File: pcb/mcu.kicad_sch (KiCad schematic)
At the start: 20 parts, among them U3 IC_MCU_STM32F100C4T6B_48LQFP, X1 XTAL_8M_20PPM_18pF_ECS-80-18-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, X2 XTAL_32K768_10PPM_7pF_ECS-.32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

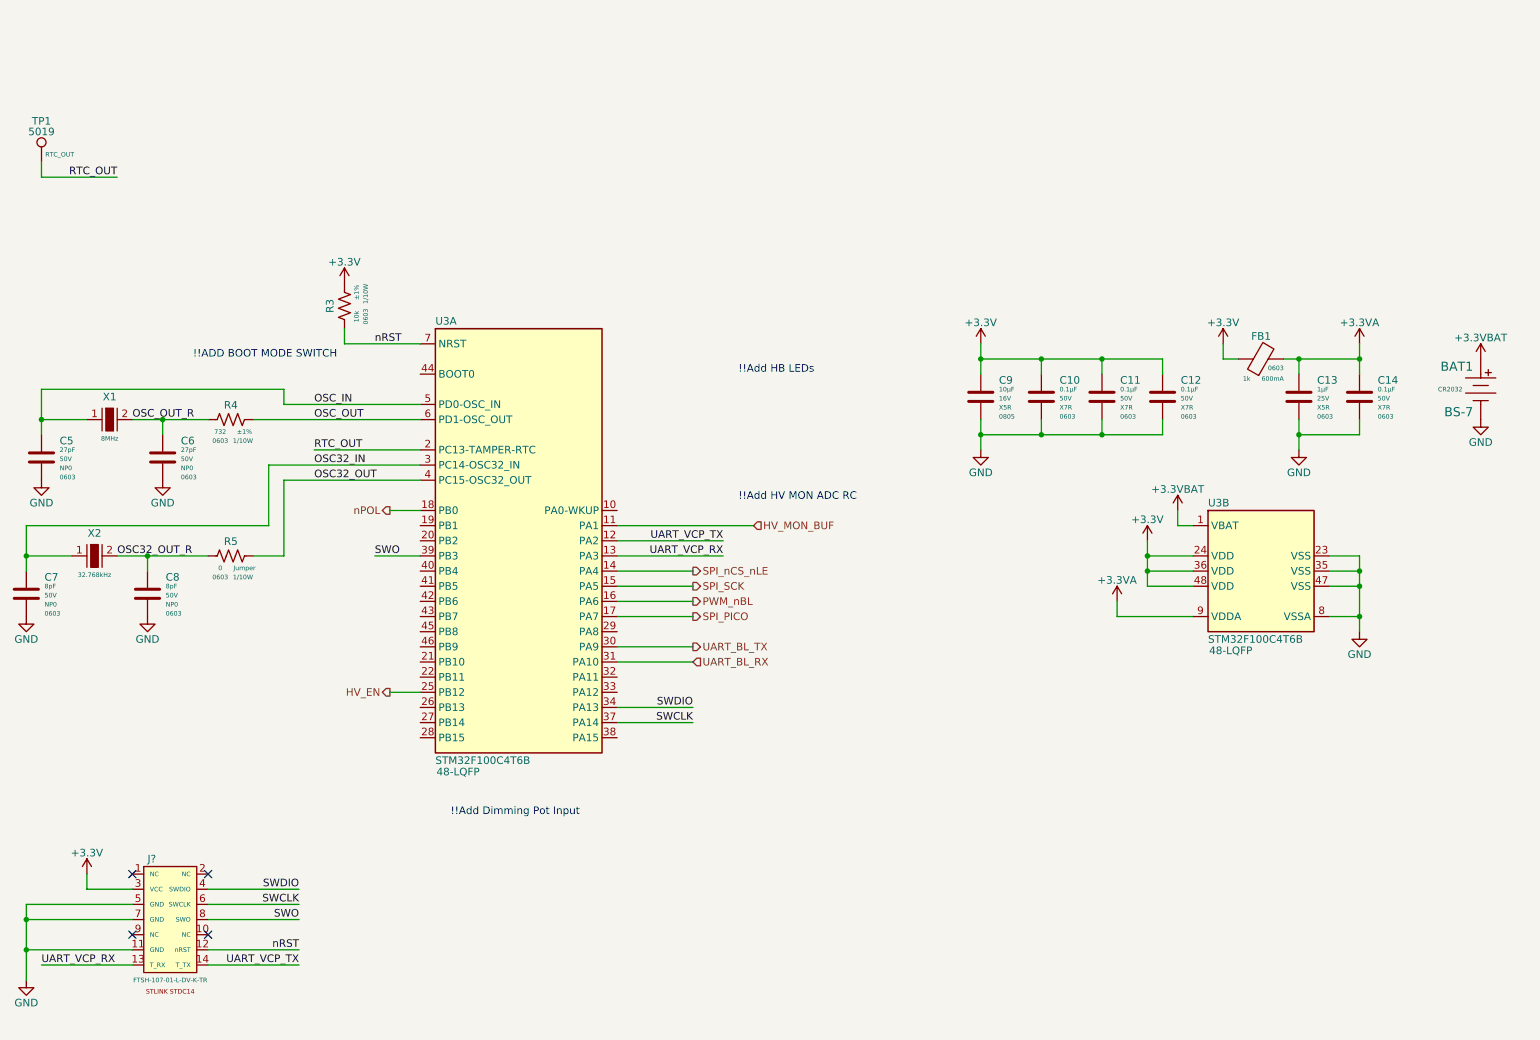
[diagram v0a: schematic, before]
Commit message: Added Boot mode selection
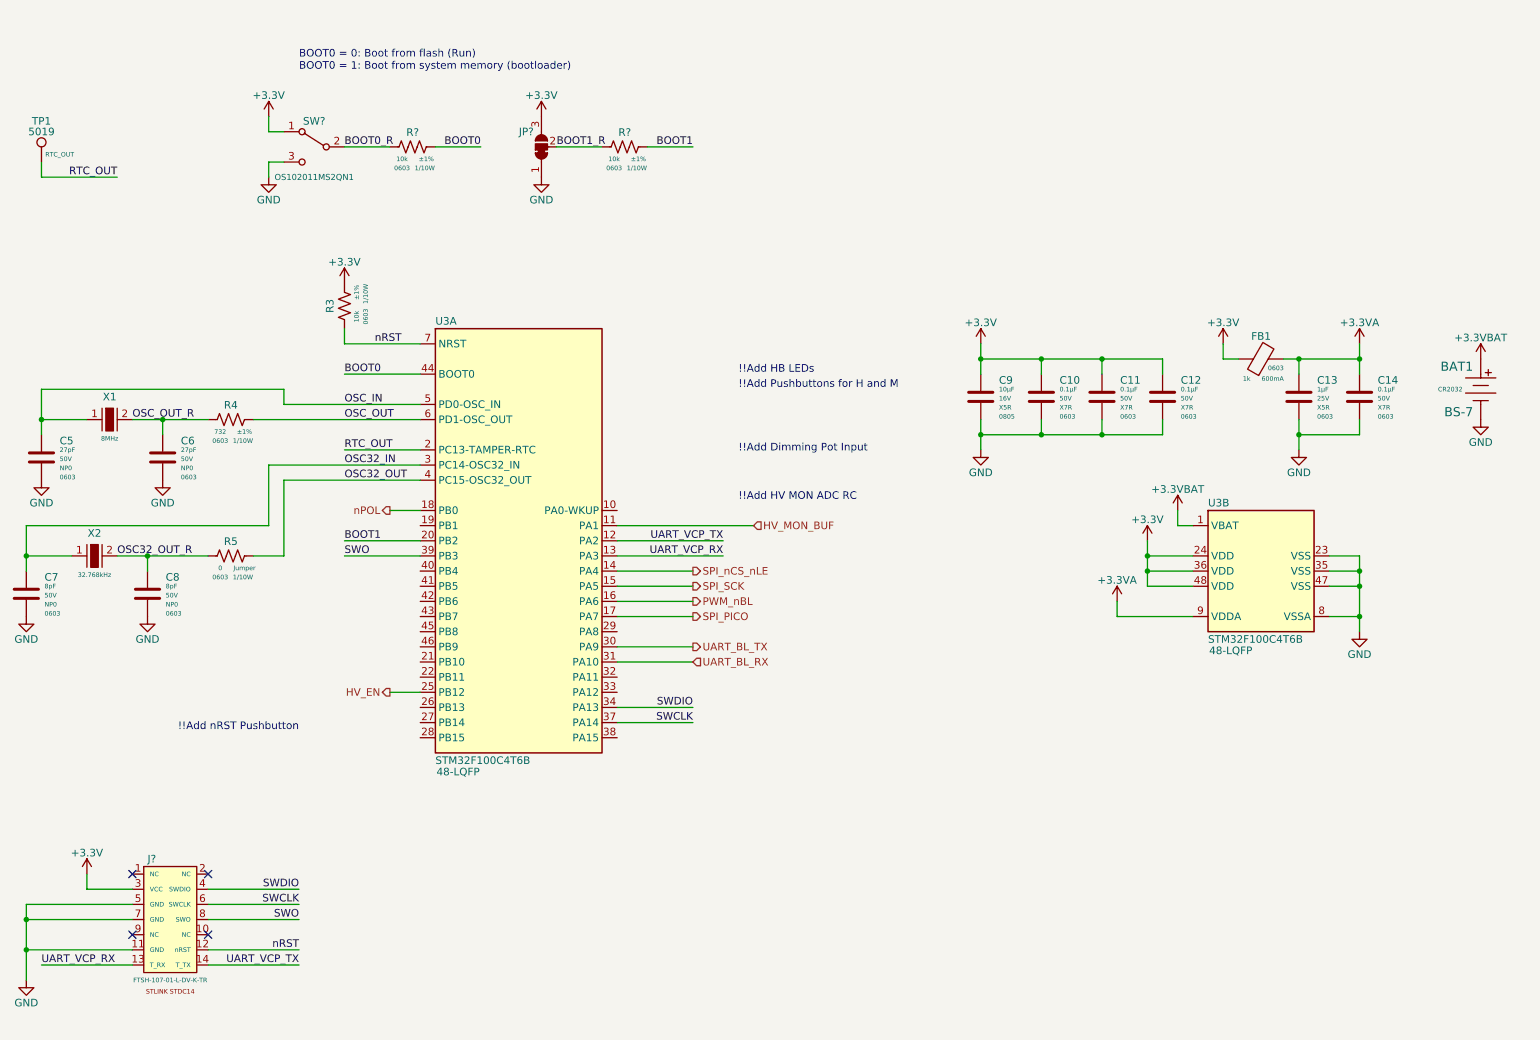
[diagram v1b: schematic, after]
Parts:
- added JP?: SolderJumper_3_Bridged12, Jumper:SolderJumper-3_P1.3mm_Bridged12_RoundedPad1.0x1.5mm_NumberLabels, symbol arjun_symbols:SolderJumper_3_Bridged12
- added R? (x2): RES_10K_1P_1/10W_0603, Resistor_SMD:R_0603_1608Metric, symbol arjun_symbols:RES_10K_1P_1/10W_0603
- added SW?: SW_SPDT_12V_100mA_OS102011MS2QN1, arjun_footprints:SW_OS102011MS2QN1, symbol arjun_symbols:SW_SPDT_12V_100mA_OS102011MS2QN1
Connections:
- net +3.3V: now also JP?.3 (B), SW?.1 (A)
- net GND: now also JP?.1 (A), SW?.3 (C)
- net BOOT1: now reaches U3.20 (PB2)
- net BOOT1: now also R?.1
- net BOOT0: now reaches U3.44 (BOOT0)
- net BOOT0: now also R?.1
- new net BOOT0_R: R?.2, SW?.2 (B)
- new net BOOT1_R: JP?.2 (C), R?.2
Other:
- note added: "!!Add Pushbuttons for H and M"
- note added: "!!Add nRST Pushbutton"
- note added: "BOOT0 = 0: Boot from flash (Run) BOOT0 = 1: Boot from system memory (bootloader)"
- note removed: "!!ADD BOOT MODE SWITCH"

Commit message: Changed Boot0 switch to mom. pb, added rotary encoder, and nRST pb
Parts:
- removed SW?: SW_SPDT_12V_100mA_OS102011MS2QN1, arjun_footprints:SW_OS102011MS2QN1, symbol arjun_symbols:SW_SPDT_12V_100mA_OS102011MS2QN1
- added S? (x2): SW_TACT_PTS645SM43SMTR92_LFS, arjun_footprints:Switch_Tactile_SMD_6x6mm_PTS645, symbol arjun_symbols:SW_TACT_PTS645SM43SMTR92_LFS
- U3: footprint Package_QFP:LQFP-48_7x7mm_P0.5mm -> arjun_footprints:LQFP-48_7x7mm_P0.5mm
- gave numbers to parts that had none: 4
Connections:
- net BOOT0_R is gone; now on net GND: R15.2
- net +3.3V: now also S?.1, S?.2
- net BOOT0: now also S?.3, S?.4
- net GND: now also S?.1, S?.2
- net nRST: now also S?.3, S?.4
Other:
- note added: "0"
- note added: "1"
- note added: "Add ESD protection"
- note added: "BOOT0"
- note added: "BOOT1"
- note added: "Boot Mode"
- note added: "Boot from embedded SRAM (likely never use)"
- note added: "Boot from flash (run)"
- note added: "Boot from system memory (bootloader)"
- note added: "X"
- note added: "add debouncing"
- note removed: "!!Add Dimming Pot Input"
- note removed: "!!Add nRST Pushbutton"
- note removed: "BOOT0 = 0: Boot from flash (Run) BOOT0 = 1: Boot from system memory (bootloader)"
- moved on the sheet: R15

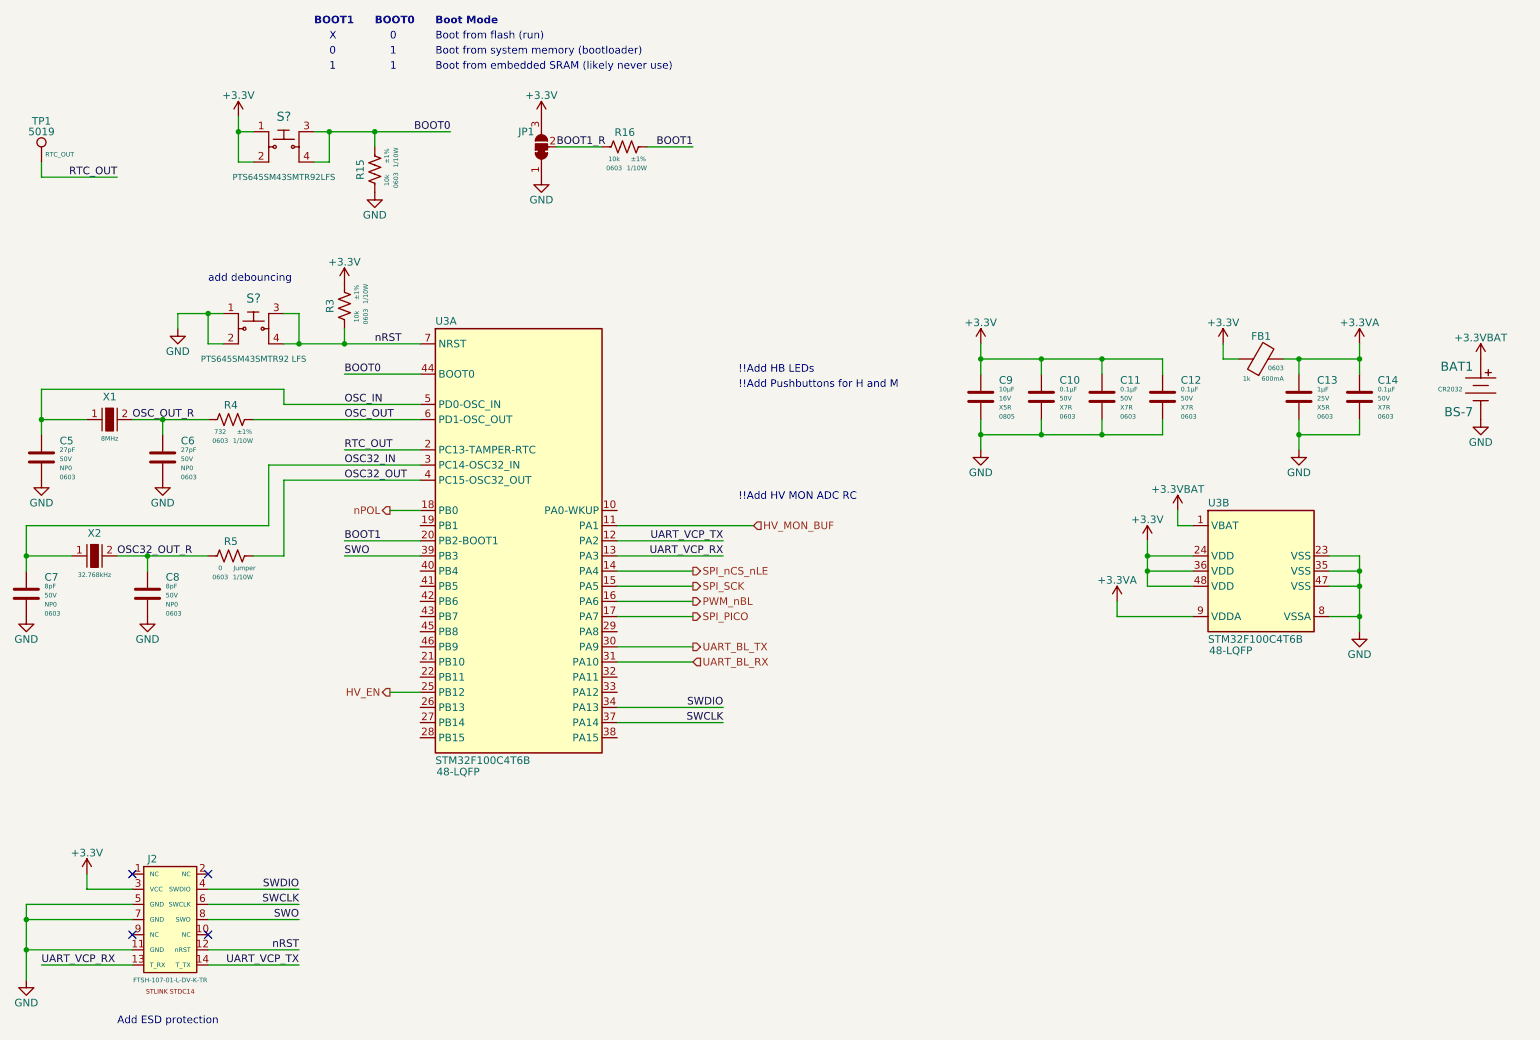
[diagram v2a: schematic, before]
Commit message: Added switch debouncing
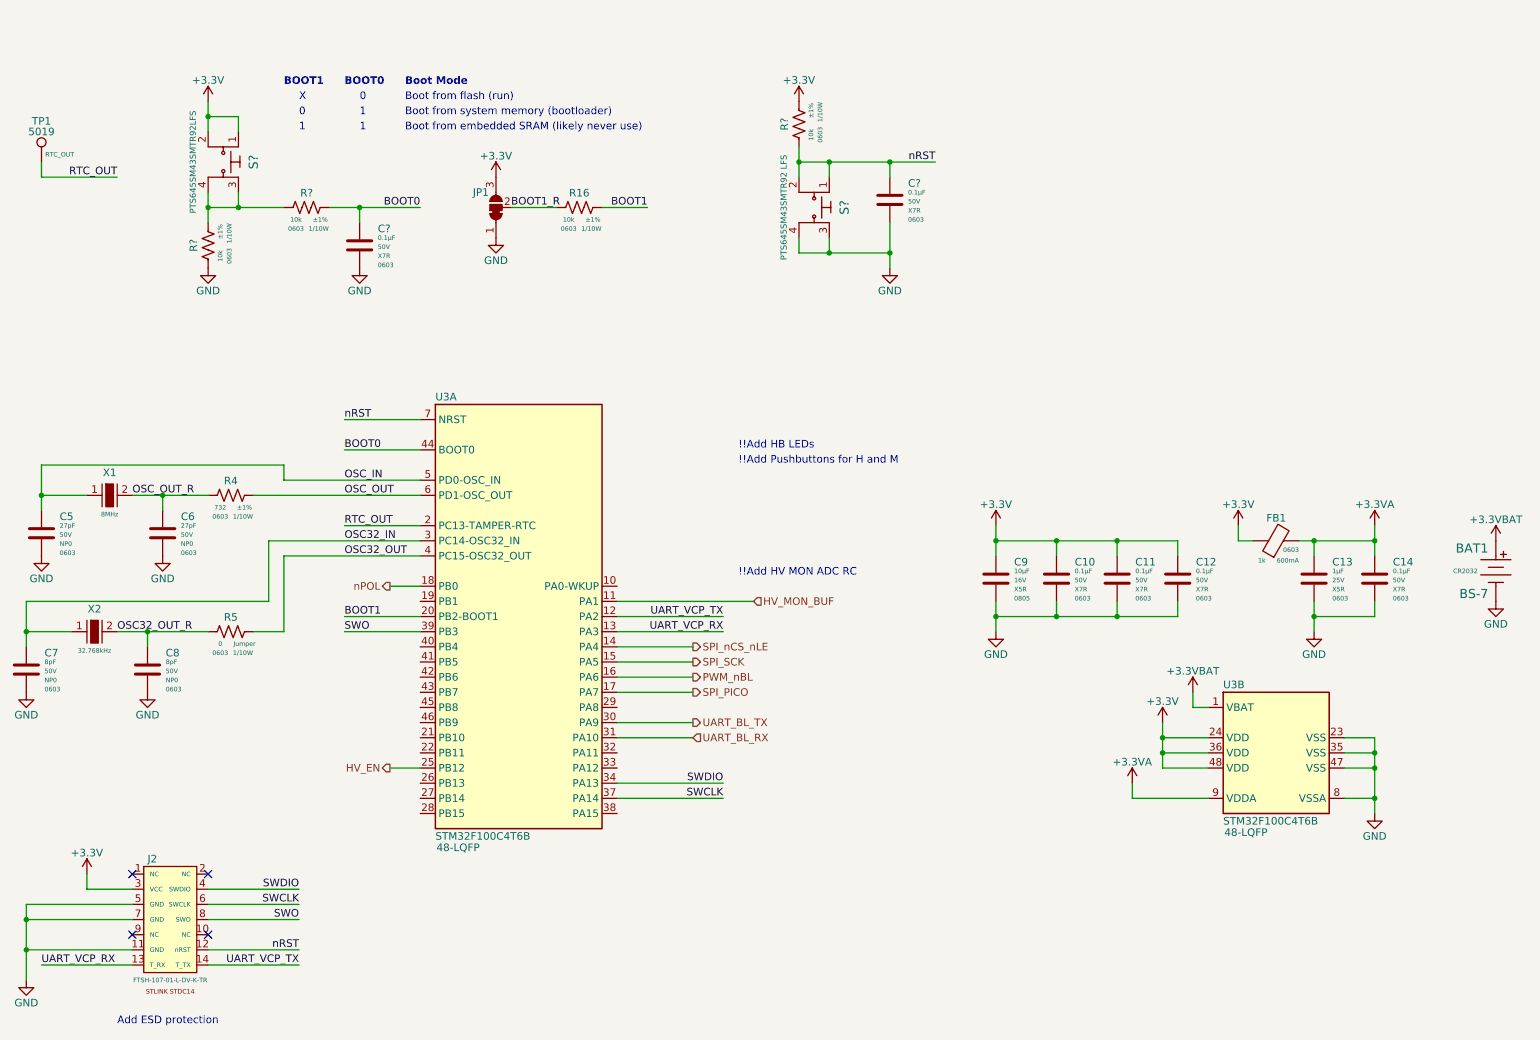
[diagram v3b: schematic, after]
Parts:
- removed R15, R3: RES_10K_1P_1/10W_0603, Resistor_SMD:R_0603_1608Metric, symbol arjun_symbols:RES_10K_1P_1/10W_0603
- removed S? (x2): SW_TACT_PTS645SM43SMTR92_LFS, arjun_footprints:Switch_Tactile_SMD_6x6mm_PTS645, symbol arjun_symbols:SW_TACT_PTS645SM43SMTR92_LFS
- added C? (x2): CAP_CER_0u1_50V_X7R_0603, Capacitor_SMD:C_0603_1608Metric, symbol arjun_symbols:CAP_CER_0u1_50V_X7R_0603
- added R? (x3): RES_10K_1P_1/10W_0603, Resistor_SMD:R_0603_1608Metric, symbol arjun_symbols:RES_10K_1P_1/10W_0603
- added S? (x2): SW_TACT_PTS645SM43SMTR92_LFS, arjun_footprints:Switch_Tactile_SMD_6x6mm_PTS645, symbol arjun_symbols:SW_TACT_PTS645SM43SMTR92_LFS
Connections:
- net +3.3V: now also R?.1, S?.1, S?.2
- net BOOT0: now also C?.1, R?.1
- net GND: now also C?.2, C?.2, R?.2, S?.3, S?.4
- net nRST: now also C?.1, R?.2, S?.1, S?.2
- new net: R?.1, R?.2, S?.3, S?.4
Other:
- note removed: "add debouncing"
- moved on the sheet: BAT1, C10, C11, C12, C13, C14, C5, C6, C7, C8, C9, FB1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

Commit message: Added MCU pinouts for rotary encoder
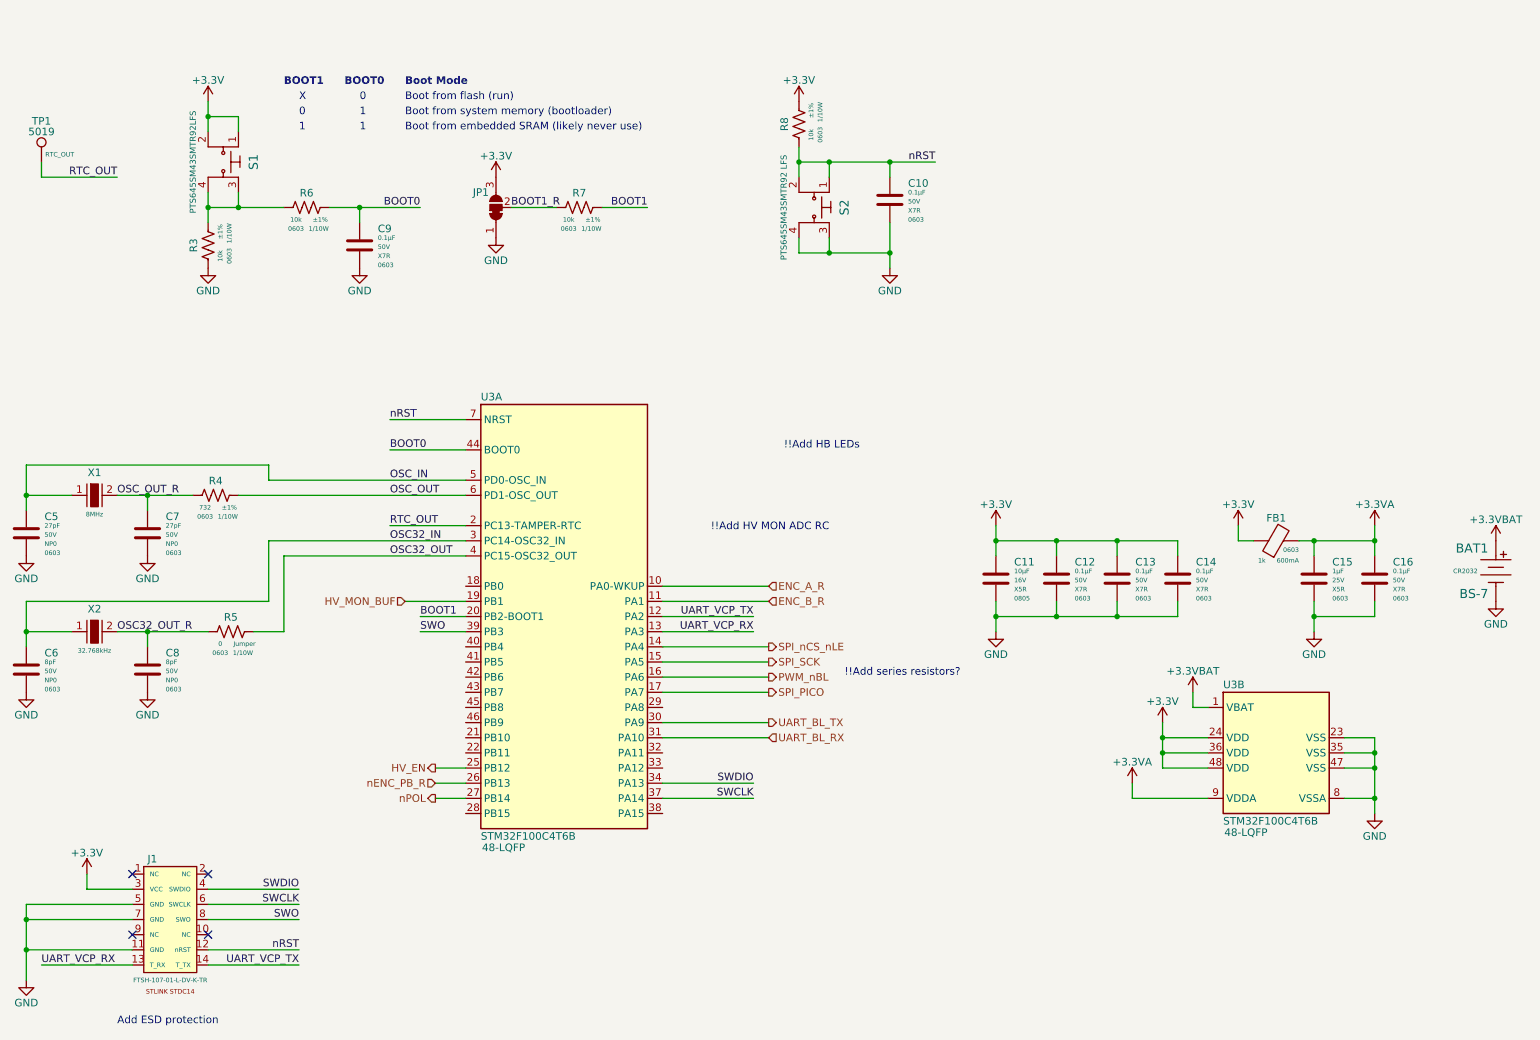
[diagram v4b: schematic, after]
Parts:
- gave numbers to parts that had none: 7
- renumbered C9 to C11, C10 to C12, C11 to C13, C12 to C14, C13 to C15, C14 to C16, C7 to C6, C6 to C7, J2 to J1, R16 to R7
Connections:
- net HV_MON_BUF: now also U3.19 (PB1); no longer U3.11 (PA1)
- net nPOL: now also U3.27 (PB14); no longer U3.18 (PB0)
- net ENC_A_R: now reaches U3.10 (PA0-WKUP)
- net nENC_PB_R: now reaches U3.26 (PB13)
- new net ENC_B_R: U3.11 (PA1)
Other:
- note added: "!!Add series resistors?"
- note removed: "!!Add Pushbuttons for H and M"
- moved on the sheet: C5, C7, R4, U3A, X1
